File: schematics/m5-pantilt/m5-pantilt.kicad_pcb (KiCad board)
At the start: 2 copper layers, 50 x 50 mm, 39 parts, among them J1 Conn_02x15_Odd_Even, J2 Conn_02x15_Odd_Even, J3 Conn_01x03, J5 BAT, J6 Conn_01x04, J7 5V_POWER, J8 Conn_01x03, Q1 IRLML6402, Q2 BC857, SW1 SW_SPDT, U1 MAX3485

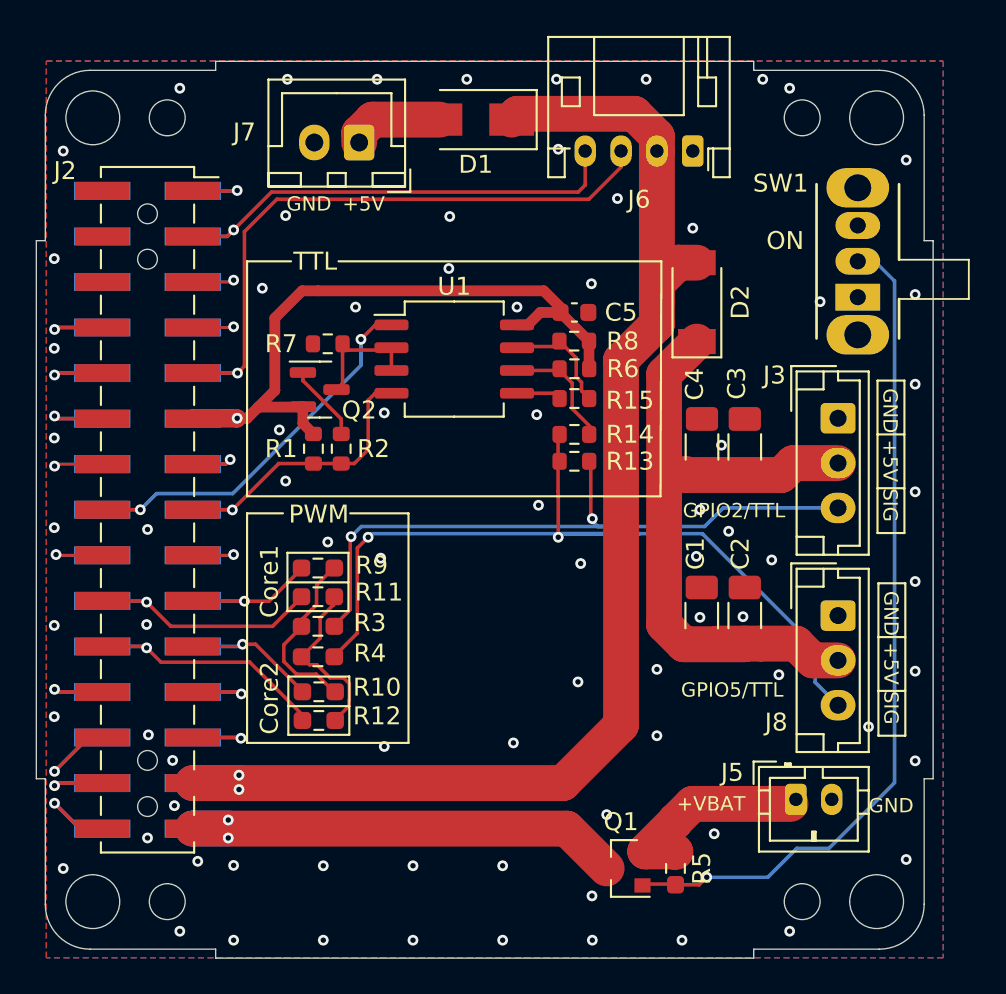
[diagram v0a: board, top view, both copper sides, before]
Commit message: 部品、いくつかのfootprint変更
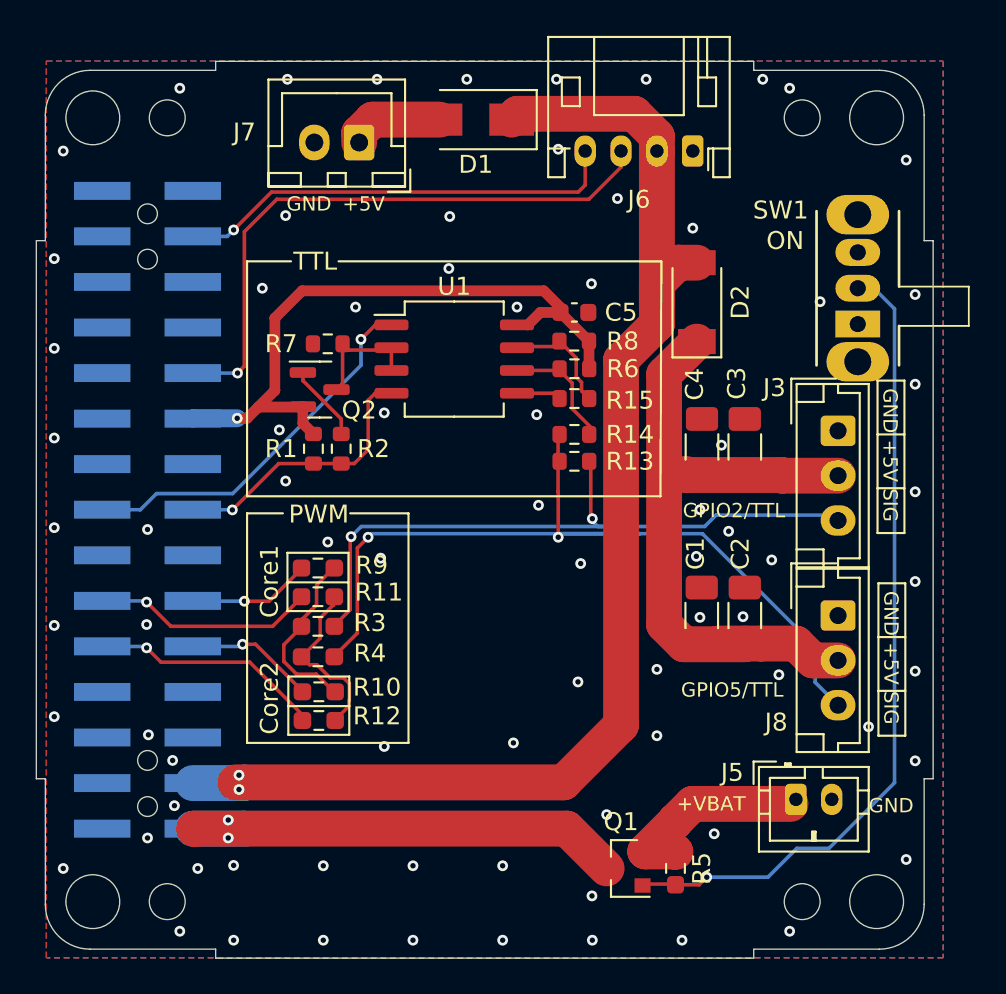
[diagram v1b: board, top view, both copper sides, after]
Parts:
- removed J2: Conn_02x15_Odd_Even, Connector_PinSocket_2.54mm:PinSocket_2x15_P2.54mm_Vertical_SMD
- moved SW1 1.50 mm to (145.8, 64.7)
- moved J3 0.70 mm to (144.7, 70.6)
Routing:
- net /PIN26: track 6.89 -> 0.00 mm, vias 1 -> 0
- net /PIN30: track 6.50 -> 0.00 mm, vias 1 -> 0
- net /PIN23: track 5.50 -> 0.00 mm, vias 1 -> 0
- net /PIN24: track 5.44 -> 0.00 mm, vias 1 -> 0
- net /PIN12: track 5.44 -> 0.00 mm, vias 1 -> 0
- net /PIN28: track 5.44 -> 0.00 mm, vias 1 -> 0
- net /PIN14: track 5.41 -> 0.00 mm, vias 1 -> 0
- net /PIN10: track 5.41 -> 0.00 mm, vias 1 -> 0
- net /PIN8: track 5.41 -> 0.00 mm, vias 1 -> 0
- net /PIN25: track 5.41 -> 0.00 mm, vias 1 -> 0
- net /PIN18: track 5.19 -> 0.00 mm, vias 1 -> 0
- net /PIN1: track 4.97 -> 0.00 mm, vias 1 -> 0
- net /PIN5: track 4.64 -> 0.00 mm, vias 1 -> 0
- net /PIN7: track 4.59 -> 0.00 mm, vias 1 -> 0
- net /PIN17: track 4.59 -> 0.00 mm, vias 1 -> 0
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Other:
- board text added: "74th-fork-1.0.1"
